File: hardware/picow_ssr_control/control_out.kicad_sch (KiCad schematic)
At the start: 12 parts

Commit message: Updated schemas
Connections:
- net BANK_A.CNTL4: now also RS4.1; no longer RS4.2
- net a4o: now also RS4.2; no longer RS4.1
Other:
- moved on the sheet: RS4
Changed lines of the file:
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@@
   (paper "USLetter")
   (title_block
-    (date "2023-01-27")
+    (date "2023-01-28")
     (rev "0.0.10")
     (comment 2 "http://creativecommons.org/licenses/by-sa/4.0/")
@@
   )
   (bus (pts (xy 53.34 68.58) (xy 53.34 73.66))
-    (stroke (width 0) (type default) (color 0 0 0 0))
+    (stroke (width 0) (type default) (color 255 255 0 1))
   )
   (wire (pts (xy 119.38 33.02) (xy 92.71 33.02))
@@
   )
   (bus (pts (xy 53.34 40.64) (xy 53.34 43.18))
-    (stroke (width 0) (type default) (color 0 0 0 0))
+    (stroke (width 0) (type default) (color 255 255 0 1))
   )
   (wire (pts (xy 92.71 33.02) (xy 92.71 40.64))
@@
   )
   (bus (pts (xy 53.34 43.18) (xy 53.34 45.72))
-    (stroke (width 0) (type default) (color 0 0 0 0))
+    (stroke (width 0) (type default) (color 255 255 0 1))
   )
   (wire (pts (xy 92.71 91.44) (xy 92.71 86.36))
@@
   )
   (bus (pts (xy 53.34 73.66) (xy 53.34 76.2))
+    (stroke (width 0) (type default) (color 255 255 0 1))
+  )
+  (wire (pts (xy 81.28 48.26) (xy 92.71 48.26))
     (stroke (width 0) (type default) (color 0 0 0 0))
   )
@@
   )
   (bus (pts (xy 50.8 35.56) (xy 53.34 35.56))
-    (stroke (width 0) (type default) (color 0 0 0 0))
+    (stroke (width 0) (type default) (color 255 255 0 1))
   )
   (bus (pts (xy 50.8 68.58) (xy 53.34 68.58))
-    (stroke (width 0) (type default) (color 0 0 0 0))
+    (stroke (width 0) (type default) (color 255 255 0 1))
   )
   (wire (pts (xy 55.88 48.26) (xy 76.2 48.26))
@@
   )
   (bus (pts (xy 53.34 45.72) (xy 53.34 48.26))
-    (stroke (width 0) (type default) (color 0 0 0 0))
+    (stroke (width 0) (type default) (color 255 255 0 1))
   )
   (wire (pts (xy 127 55.88) (xy 127 66.04))
@@
   )
   (bus (pts (xy 53.34 76.2) (xy 53.34 78.74))
-    (stroke (width 0) (type default) (color 0 0 0 0))
+    (stroke (width 0) (type default) (color 255 255 0 1))
   )
   (bus (pts (xy 53.34 35.56) (xy 53.34 40.64))
-    (stroke (width 0) (type default) (color 0 0 0 0))
+    (stroke (width 0) (type default) (color 255 255 0 1))
   )
   (wire (pts (xy 127 55.88) (xy 132.08 55.88))
@@
     (stroke (width 0) (type default) (color 0 0 0 0))
   )
-  (wire (pts (xy 92.71 48.26) (xy 81.28 48.26))
-    (stroke (width 0) (type default) (color 0 0 0 0))
-  )
   (wire (pts (xy 92.71 50.8) (xy 86.36 50.8))
     (stroke (width 0) (type default) (color 0 0 0 0))
@@
   )
   (bus (pts (xy 53.34 78.74) (xy 53.34 81.28))
-    (stroke (width 0) (type default) (color 0 0 0 0))
+    (stroke (width 0) (type default) (color 255 255 0 1))
   )
   (wire (pts (xy 106.68 50.8) (xy 106.68 55.88))
@@
     (pin "2")
   )
-  (symbol (lib_id "Device:R_Small") (at 83.82 50.8 270) (unit 1)
+  (symbol (lib_name "R_Small_1") (lib_id "Device:R_Small") (at 83.82 50.8 90) (unit 1)
     (in_bom yes) (on_board yes)
     (property "Reference" "RS4" (id 0) (at 83.82 49.276 90)
@@
     (pin "1")
   )
-  (symbol (lib_id "Device:R_Small") (at 83.82 83.82 90) (mirror x) (unit 1)
+  (symbol (lib_name "R_Small_2") (lib_id "Device:R_Small") (at 83.82 83.82 90) (mirror x) (unit 1)
     (in_bom yes) (on_board yes)
     (property "Reference" "RS5" (id 0) (at 83.82 82.296 90)

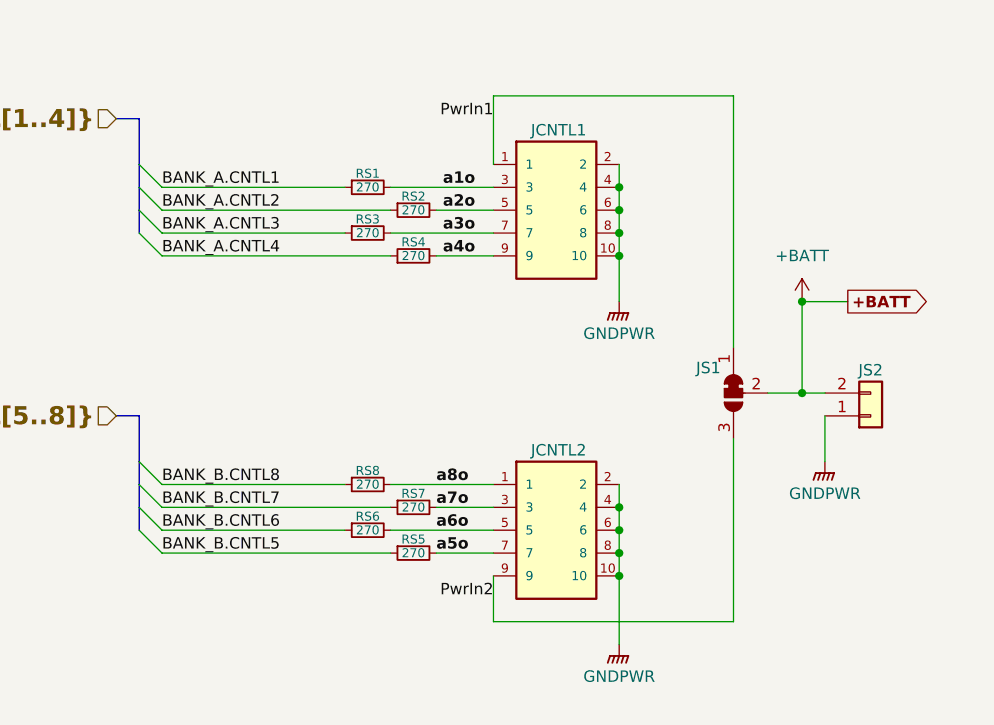
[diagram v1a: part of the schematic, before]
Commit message: Power supply changes plus misc.
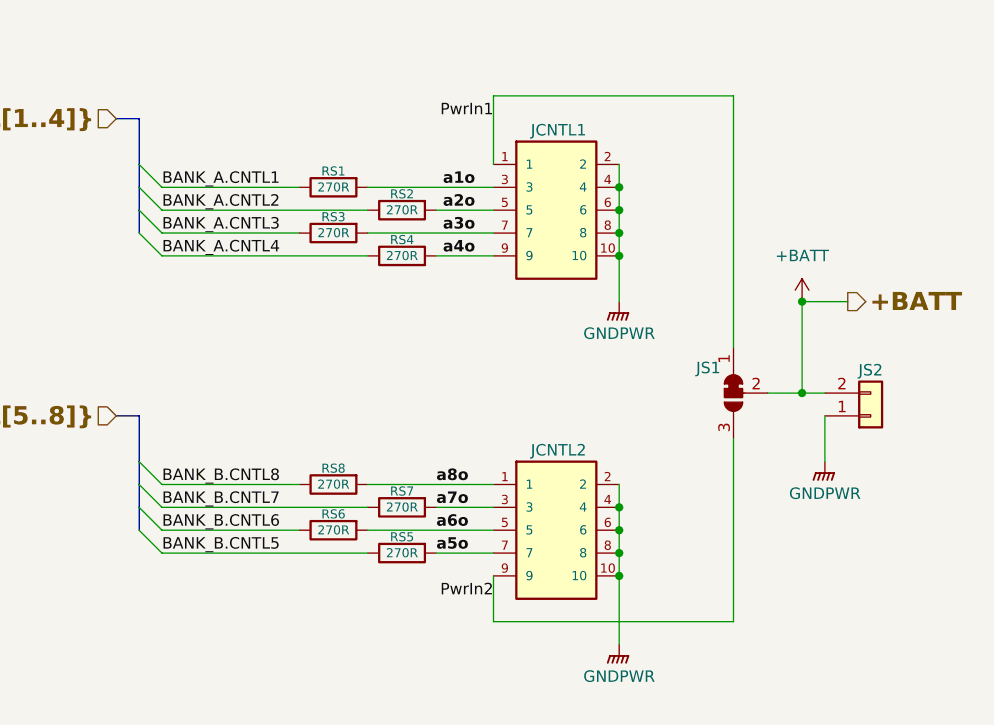
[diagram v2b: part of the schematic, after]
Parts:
- JCNTL1, JCNTL2: Characteristics (none) -> Headers & Wire Housings Shrouded Terminal Strip, 0.050"(1.2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; Package (none) -> Other
- JS2: footprint Connector_PinHeader_1.00mm:PinHeader_1x02_P1.00mm_Vertical -> dragon_mobile:PinHeader_1x02_P1.00mm_Vertical; Characteristics (none) -> Pin Header; 1mm 1x2 Vertical
- RS1, RS2, RS3, RS4, RS5, RS6, RS7, RS8: value 270 -> 270R; symbol Device:R_Small -> Device:R; Height (mm) (none) -> 0.45
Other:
- moved on the sheet: RS1, RS2, RS3, RS4, RS5, RS6, RS7, RS8

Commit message: Pre KiCad 7.0.0 WIP
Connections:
- net BANK_A.CNTL1 renamed BANK_A.OUT1
- net BANK_A.CNTL2 renamed BANK_A.OUT2
- net BANK_A.CNTL3 renamed BANK_A.OUT3
- net BANK_A.CNTL4 renamed BANK_A.OUT4
- net BANK_B.CNTL5 renamed BANK_B.OUT5
- net BANK_B.CNTL6 renamed BANK_B.OUT6
- net BANK_B.CNTL7 renamed BANK_B.OUT7
- net BANK_B.CNTL8 renamed BANK_B.OUT8
- net a1o renamed OUT1
- net a2o renamed OUT2
- net a3o renamed OUT3
- net a4o renamed OUT4
- net a5o renamed OUT5
- net a6o renamed OUT6
- net a7o renamed OUT7
- net a8o renamed OUT8
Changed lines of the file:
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@@
     (comment 6 "Hardware License: CERN-OHL-W")
   )
-  (junction (at 106.68 86.36) (diameter 0) (color 0 0 0 0)
-  )
   (junction (at 127 66.04) (diameter 0) (color 0 0 0 0)
   )
@@
   (junction (at 127 55.88) (diameter 0) (color 0 0 0 0)
   )
+  (junction (at 106.68 76.2) (diameter 0) (color 0 0 0 0)
+  )
   (junction (at 106.68 48.26) (diameter 0) (color 0 0 0 0)
   )
@@
     (stroke (width 0) (type default) (color 0 0 0 0))
   )
+  (wire (pts (xy 111.76 78.74) (xy 111.76 76.2))
+    (stroke (width 0) (type default) (color 0 0 0 0))
+  )
   (bus (pts (xy 53.34 68.58) (xy 53.34 73.66))
     (stroke (width 0) (type default) (color 255 255 0 1))
@@
     (stroke (width 0) (type default) (color 0 0 0 0))
   )
-  (wire (pts (xy 106.68 86.36) (xy 106.68 93.98))
-    (stroke (width 0) (type default) (color 0 0 0 0))
-  )
   (bus (pts (xy 53.34 45.72) (xy 53.34 48.26))
     (stroke (width 0) (type default) (color 255 255 0 1))
@@
   )
   (wire (pts (xy 106.68 45.72) (xy 106.68 48.26))
+    (stroke (width 0) (type default) (color 0 0 0 0))
+  )
+  (wire (pts (xy 111.76 76.2) (xy 106.68 76.2))
     (stroke (width 0) (type default) (color 0 0 0 0))
   )
@@
     (effects (font (size 4 4) bold) (justify left bottom))
   )
-  (label "BANK_B.CNTL5" (at 55.88 83.82 0)
-    (effects (font (size 1.27 1.27)) (justify left bottom))
-  )
-  (label "BANK_B.CNTL7" (at 55.88 78.74 0)
-    (effects (font (size 1.27 1.27)) (justify left bottom))
-  )
-  (label "BANK_A.CNTL1" (at 55.88 43.18 0)
-    (effects (font (size 1.27 1.27)) (justify left bottom))
-  )
-  (label "BANK_A.CNTL3" (at 55.88 48.26 0)
-    (effects (font (size 1.27 1.27)) (justify left bottom))
-  )
-  (label "a5o" (at 86.36 83.82 0)
+  (label "BANK_B.OUT5" (at 55.88 83.82 0)
+    (effects (font (size 1.27 1.27)) (justify left bottom))
+  )
+  (label "BANK_B.OUT7" (at 55.88 78.74 0)
+    (effects (font (size 1.27 1.27)) (justify left bottom))
+  )
+  (label "BANK_A.OUT1" (at 55.88 43.18 0)
+    (effects (font (size 1.27 1.27)) (justify left bottom))
+  )
+  (label "BANK_A.OUT3" (at 55.88 48.26 0)
+    (effects (font (size 1.27 1.27)) (justify left bottom))
+  )
+  (label "OUT5" (at 86.36 83.82 0)
     (effects (font (size 1.27 1.27) bold) (justify left bottom))
   )
-  (label "BANK_B.CNTL8" (at 55.88 76.2 0)
-    (effects (font (size 1.27 1.27)) (justify left bottom))
-  )
-  (label "BANK_B.CNTL6" (at 55.88 81.28 0)
-    (effects (font (size 1.27 1.27)) (justify left bottom))
-  )
-  (label "BANK_A.CNTL4" (at 55.88 50.8 0)
-    (effects (font (size 1.27 1.27)) (justify left bottom))
-  )
-  (label "a2o" (at 90.678 45.72 180)
-    (effects (font (size 1.27 1.27) (thickness 0.254) bold) (justify right bottom))
+  (label "BANK_B.OUT8" (at 55.88 76.2 0)
+    (effects (font (size 1.27 1.27)) (justify left bottom))
+  )
+  (label "BANK_B.OUT6" (at 55.88 81.28 0)
+    (effects (font (size 1.27 1.27)) (justify left bottom))
+  )
+  (label "BANK_A.OUT4" (at 55.88 50.8 0)
+    (effects (font (size 1.27 1.27)) (justify left bottom))
+  )
+  (label "OUT2" (at 86.36 45.72 0)
+    (effects (font (size 1.27 1.27) (thickness 0.254) bold) (justify left bottom))
   )
   (label "PwrIn1" (at 92.71 35.56 180)
@@
     (effects (font (size 1.27 1.27)) (justify right bottom))
   )
-  (label "a4o" (at 90.678 50.8 180)
-    (effects (font (size 1.27 1.27) (thickness 0.254) bold) (justify right bottom))
-  )
-  (label "a3o" (at 90.678 48.26 180)
-    (effects (font (size 1.27 1.27) (thickness 0.254) bold) (justify right bottom))
-  )
-  (label "BANK_A.CNTL2" (at 55.88 45.72 0)
-    (effects (font (size 1.27 1.27)) (justify left bottom))
-  )
-  (label "a7o" (at 86.36 78.74 0)
+  (label "OUT4" (at 86.36 50.8 0)
+    (effects (font (size 1.27 1.27) (thickness 0.254) bold) (justify left bottom))
+  )
+  (label "OUT3" (at 86.36 48.26 0)
+    (effects (font (size 1.27 1.27) (thickness 0.254) bold) (justify left bottom))
+  )
+  (label "BANK_A.OUT2" (at 55.88 45.72 0)
+    (effects (font (size 1.27 1.27)) (justify left bottom))
+  )
+  (label "OUT7" (at 86.36 78.74 0)
     (effects (font (size 1.27 1.27) bold) (justify left bottom))
   )
-  (label "a6o" (at 86.36 81.28 0)
+  (label "OUT6" (at 86.36 81.28 0)
     (effects (font (size 1.27 1.27) bold) (justify left bottom))
   )
-  (label "a1o" (at 90.678 43.18 180)
-    (effects (font (size 1.27 1.27) (thickness 0.254) bold) (justify right bottom))
-  )
-  (label "a8o" (at 86.36 76.2 0)
+  (label "OUT1" (at 86.36 43.18 0)
+    (effects (font (size 1.27 1.27) (thickness 0.254) bold) (justify left bottom))
+  )
+  (label "OUT8" (at 86.36 76.2 0)
     (effects (font (size 1.27 1.27) bold) (justify left bottom))
   )
-  (hierarchical_label "BANK_B{CNTL[5..8]}" (shape input) (at 50.8 68.58 180)
+  (hierarchical_label "BANK_B{OUT[5..8]}" (shape input) (at 50.8 68.58 180)
     (effects (font (size 2 2) bold) (justify right))
   )
-  (hierarchical_label "BANK_A{CNTL[1..4]}" (shape input) (at 50.8 35.56 180)
+  (hierarchical_label "BANK_A{OUT[1..4]}" (shape input) (at 50.8 35.56 180)
     (effects (font (size 2 2) bold) (justify right))
   )
@@
     (pin "2")
   )
-  (symbol (lib_id "power:GNDPWR") (at 106.68 93.98 0) (unit 1)
-    (in_bom yes) (on_board yes)
-    (property "Reference" "#PWR011" (id 0) (at 106.68 99.06 0)
-      (effects (font (size 1.27 1.27)) hide)
-    )
-    (property "Value" "GNDPWR" (id 1) (at 106.68 97.536 0))
-    (property "Footprint" "" (id 2) (at 106.68 95.25 0)
-      (effects (font (size 1.27 1.27)) hide)
-    )
-    (property "Datasheet" "" (id 3) (at 106.68 95.25 0)
-      (effects (font (size 1.27 1.27)) hide)
-    )
+  (symbol (lib_id "power:GNDPWR") (at 111.76 78.74 0) (unit 1)
+    (in_bom yes) (on_board yes)
+    (property "Reference" "#PWR011" (id 0) (at 111.76 83.82 0)
+      (effects (font (size 1.27 1.27)) hide)
+    )
+    (property "Value" "GNDPWR" (id 1) (at 111.76 82.296 0))
+    (property "Footprint" "" (id 2) (at 111.76 80.01 0)
+      (effects (font (size 1.27 1.27)) hide)
+    )
+    (property "Datasheet" "" (id 3) (at 111.76 80.01 0)
+      (effects (font (size 1.27 1.27)) hide)
+    )

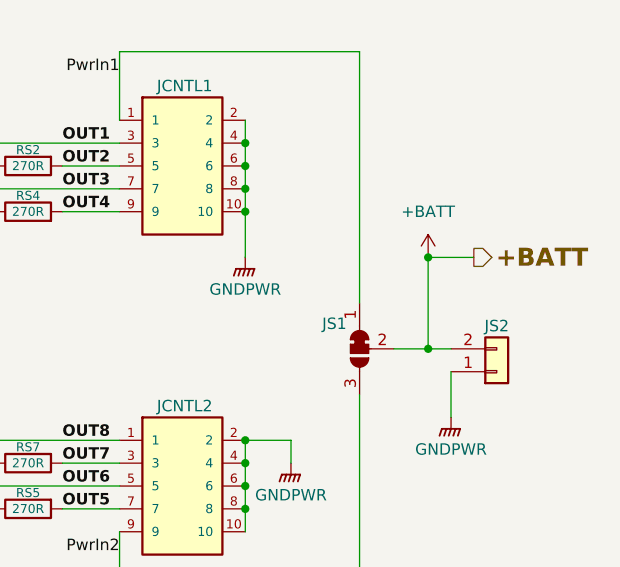
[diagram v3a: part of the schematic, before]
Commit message: Commit before trying changes to power system
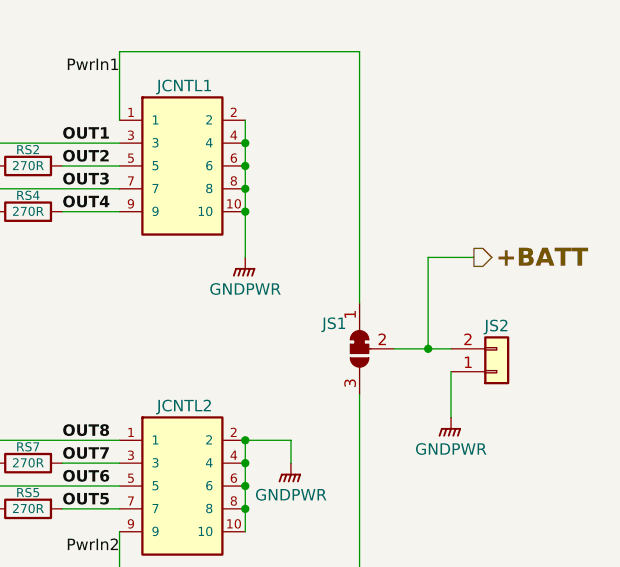
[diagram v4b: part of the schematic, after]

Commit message: Commit before removing git submodule
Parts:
- removed JS1: SolderJumper_3_Bridged12, Jumper:SolderJumper-3_P1.3mm_Bridged12_RoundedPad1.0x1.5mm_NumberLabels, symbol Jumper:SolderJumper_3_Bridged12
- removed JS2: Conn_01x02, dragon_mobile:PinHeader_1x02_P1.00mm_Vertical, symbol Connector_Generic:Conn_01x02
- renumbered JCNTL1 to JCTL1, JCNTL2 to JCTL2
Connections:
- net PwrIn1 renamed PI1
- net PwrIn2 renamed PI2
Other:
- note added: "${SHEETNAME}"
- note removed: "Control Out / Power In"
- company: (none) -> Michael Cummings
- title: (none) -> Pico W SSR Control
